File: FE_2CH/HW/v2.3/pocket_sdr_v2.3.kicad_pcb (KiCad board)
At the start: 4 copper layers, 55 x 21.6 mm, 80 parts, among them J1 PINH_2MM_2P, J2 USB_C_Receptacle_USB2.0, J4 SMA-ANG, U1 MAX2771, U2 MAX2771, U3 CY7C68013A-56LTXCT, U4 AT24C128C, U5 LDO 3.3V 500mA SOT23-5

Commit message: Fix USB-C footprint assignment
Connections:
- C10 pad 2: GND -> CPAD_2.2MM
- C11 pad 2: GND -> CPAD_2.2MM
- C13 pad 2: GND -> CPAD_2.2MM
- C14 pad 1: GND -> CPAD_2.2MM
- C16 pad 2: GND -> CPAD_2.2MM
- C17 pad 2: GND -> CPAD_2.2MM
- C18 pad 2: GND -> CPAD_2.2MM
- C19 pad 1: GND -> CPAD_2.2MM
- C2 pad 1: GND -> CPAD_2.2MM
- C20 pad 1: GND -> CPAD_2.2MM
- C21 pad 2: GND -> CPAD_2.2MM
- C22 pad P$2: GND -> CPAD_2.2MM
- C23 pad 2: GND -> CPAD_2.2MM
- C24 pad P$2: GND -> CPAD_2.2MM
- C25 pad 2: GND -> CPAD_2.2MM
- C26 pad 2: GND -> CPAD_2.2MM
- C27 pad 2: GND -> CPAD_2.2MM
- C28 pad 2: GND -> CPAD_2.2MM
- C29 pad 2: GND -> CPAD_2.2MM
- C30 pad 2: GND -> CPAD_2.2MM
- C31 pad 2: GND -> CPAD_2.2MM
- C32 pad 2: GND -> CPAD_2.2MM
- C33 pad 2: GND -> CPAD_2.2MM
- C34 pad 2: GND -> CPAD_2.2MM
- C35 pad 2: GND -> CPAD_2.2MM
- C36 pad 2: GND -> CPAD_2.2MM
- C37 pad 2: GND -> CPAD_2.2MM
- C38 pad 2: GND -> CPAD_2.2MM
- C39 pad 2: GND -> CPAD_2.2MM
- C4 pad 2: GND -> CPAD_2.2MM
- C40 pad 2: GND -> CPAD_2.2MM
- C41 pad 2: GND -> CPAD_2.2MM
- C42 pad 2: GND -> CPAD_2.2MM
- C43 pad 1: GND -> CPAD_2.2MM
- C6 pad 2: GND -> CPAD_2.2MM
- C7 pad 2: GND -> CPAD_2.2MM
- J2 pad A1: GND -> CPAD_2.2MM
- J2 pad A12: GND -> CPAD_2.2MM
- J2 pad B1: GND -> CPAD_2.2MM
- J2 pad B12: GND -> CPAD_2.2MM
- J2 pad S1: GND -> CPAD_2.2MM
- J4 pad P2: GND -> CPAD_2.2MM
- J4 pad P3: GND -> CPAD_2.2MM
- J4 pad P4: GND -> CPAD_2.2MM
- J4 pad P5: GND -> CPAD_2.2MM
- LED1 pad 2: GND -> CPAD_2.2MM
- LED2 pad 2: GND -> CPAD_2.2MM
- LED3 pad 2: GND -> CPAD_2.2MM
- R12 pad 1: GND -> CPAD_2.2MM
- R13 pad 1: GND -> CPAD_2.2MM
- RF-SHEILD-CASE0 pad P1: GND -> CPAD_2.2MM
- RF-SHEILD-CASE0 pad P10: GND -> CPAD_2.2MM
- RF-SHEILD-CASE0 pad P11: GND -> CPAD_2.2MM
- RF-SHEILD-CASE0 pad P12: GND -> CPAD_2.2MM
- RF-SHEILD-CASE0 pad P2: GND -> CPAD_2.2MM
- RF-SHEILD-CASE0 pad P3: GND -> CPAD_2.2MM
- RF-SHEILD-CASE0 pad P4: GND -> CPAD_2.2MM
- RF-SHEILD-CASE0 pad P5: GND -> CPAD_2.2MM
- RF-SHEILD-CASE0 pad P6: GND -> CPAD_2.2MM
- RF-SHEILD-CASE0 pad P7: GND -> CPAD_2.2MM
- RF-SHEILD-CASE0 pad P8: GND -> CPAD_2.2MM
- RF-SHEILD-CASE0 pad P9: GND -> CPAD_2.2MM
- RF_DIVIDER0 pad 1: GND -> CPAD_2.2MM
- RF_DIVIDER0 pad 3: GND -> CPAD_2.2MM
- RF_DIVIDER0 pad 5: GND -> CPAD_2.2MM
- TCXO0 pad 1: GND -> CPAD_2.2MM
- TCXO0 pad 2: GND -> CPAD_2.2MM
- U1 pad 20: GND -> CPAD_2.2MM
- U1 pad 26: GND -> CPAD_2.2MM
- U1 pad 5: GND -> CPAD_2.2MM
- U1 pad C1: GND -> CPAD_2.2MM
- U1 pad C2: GND -> CPAD_2.2MM
- U1 pad C3: GND -> CPAD_2.2MM
- U1 pad C4: GND -> CPAD_2.2MM
- U1 pad EP: GND -> CPAD_2.2MM
- U1 pad V1: GND -> CPAD_2.2MM
- U1 pad V2: GND -> CPAD_2.2MM
- U1 pad V3: GND -> CPAD_2.2MM
- U1 pad V4: GND -> CPAD_2.2MM
- U1 pad V5: GND -> CPAD_2.2MM
- U1 pad V6: GND -> CPAD_2.2MM
- U1 pad V7: GND -> CPAD_2.2MM
- U1 pad V8: GND -> CPAD_2.2MM
- U1 pad V9: GND -> CPAD_2.2MM
- U2 pad 19: GND -> CPAD_2.2MM
- U2 pad 25: GND -> CPAD_2.2MM
- U2 pad C1: GND -> CPAD_2.2MM
- U2 pad C2: GND -> CPAD_2.2MM
- U2 pad C3: GND -> CPAD_2.2MM
- U2 pad C4: GND -> CPAD_2.2MM
- U2 pad EP: GND -> CPAD_2.2MM
- U2 pad V1: GND -> CPAD_2.2MM
- U2 pad V2: GND -> CPAD_2.2MM
- U2 pad V3: GND -> CPAD_2.2MM
- U2 pad V4: GND -> CPAD_2.2MM
- U2 pad V5: GND -> CPAD_2.2MM
- U2 pad V6: GND -> CPAD_2.2MM
- U2 pad V7: GND -> CPAD_2.2MM
- U2 pad V8: GND -> CPAD_2.2MM
- U2 pad V9: GND -> CPAD_2.2MM
- U3 pad EP1: GND -> CPAD_2.2MM
- U3 pad EP2: GND -> CPAD_2.2MM
- U3 pad EP3: GND -> CPAD_2.2MM
- U3 pad EP4: GND -> CPAD_2.2MM
- U3 pad EP5: GND -> CPAD_2.2MM
- U3 pad P$1: GND -> CPAD_2.2MM
- U3 pad P$10: GND -> CPAD_2.2MM
- U3 pad P$11: GND -> CPAD_2.2MM
- U3 pad P$12: GND -> CPAD_2.2MM
- U3 pad P$13: GND -> CPAD_2.2MM
- U3 pad P$14: GND -> CPAD_2.2MM
- U3 pad P$15: GND -> CPAD_2.2MM
- U3 pad P$16: GND -> CPAD_2.2MM
- U3 pad P$17: GND -> CPAD_2.2MM
- U3 pad P$18: GND -> CPAD_2.2MM
- U3 pad P$19: GND -> CPAD_2.2MM
- U3 pad P$2: GND -> CPAD_2.2MM
- U3 pad P$20: GND -> CPAD_2.2MM
- U3 pad P$3: GND -> CPAD_2.2MM
- U3 pad P$4: GND -> CPAD_2.2MM
- U3 pad P$5: GND -> CPAD_2.2MM
- U3 pad P$6: GND -> CPAD_2.2MM
- U3 pad P$7: GND -> CPAD_2.2MM
- U3 pad P$8: GND -> CPAD_2.2MM
- U3 pad P$9: GND -> CPAD_2.2MM
- U3 pad P10: GND -> CPAD_2.2MM
- U3 pad P12: GND -> CPAD_2.2MM
- U3 pad P14: GND -> CPAD_2.2MM
- U3 pad P2: GND -> CPAD_2.2MM
- U3 pad P26: GND -> CPAD_2.2MM
- U3 pad P28: GND -> CPAD_2.2MM
- U3 pad P37: GND -> CPAD_2.2MM
- U3 pad P41: GND -> CPAD_2.2MM
- U3 pad P53: GND -> CPAD_2.2MM
- U3 pad P56: GND -> CPAD_2.2MM
- U3 pad P6: GND -> CPAD_2.2MM
- U4 pad 2: GND -> CPAD_2.2MM
- U4 pad 3: GND -> CPAD_2.2MM
- U4 pad 4: GND -> CPAD_2.2MM
- U4 pad 7: GND -> CPAD_2.2MM
- U5 pad 2: GND -> CPAD_2.2MM
- XTAL0 pad P2: GND -> CPAD_2.2MM
- XTAL0 pad P4: GND -> CPAD_2.2MM
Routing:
- net GND: track 1.18 -> 0.00 mm, vias 155 -> 0
- net CPAD_2.2MM: track 0.00 -> 1.18 mm, vias 0 -> 155
- added copper zone on B.Cu, net CPAD_2.2MM
- added copper zone on F.Cu, net CPAD_2.2MM
- added copper zone on In1.Cu, net CPAD_2.2MM
- added copper zone on In2.Cu, net CPAD_2.2MM
- removed copper zone on B.Cu, net GND
- removed copper zone on F.Cu, net GND
- removed copper zone on In1.Cu, net GND
- removed copper zone on In2.Cu, net GND

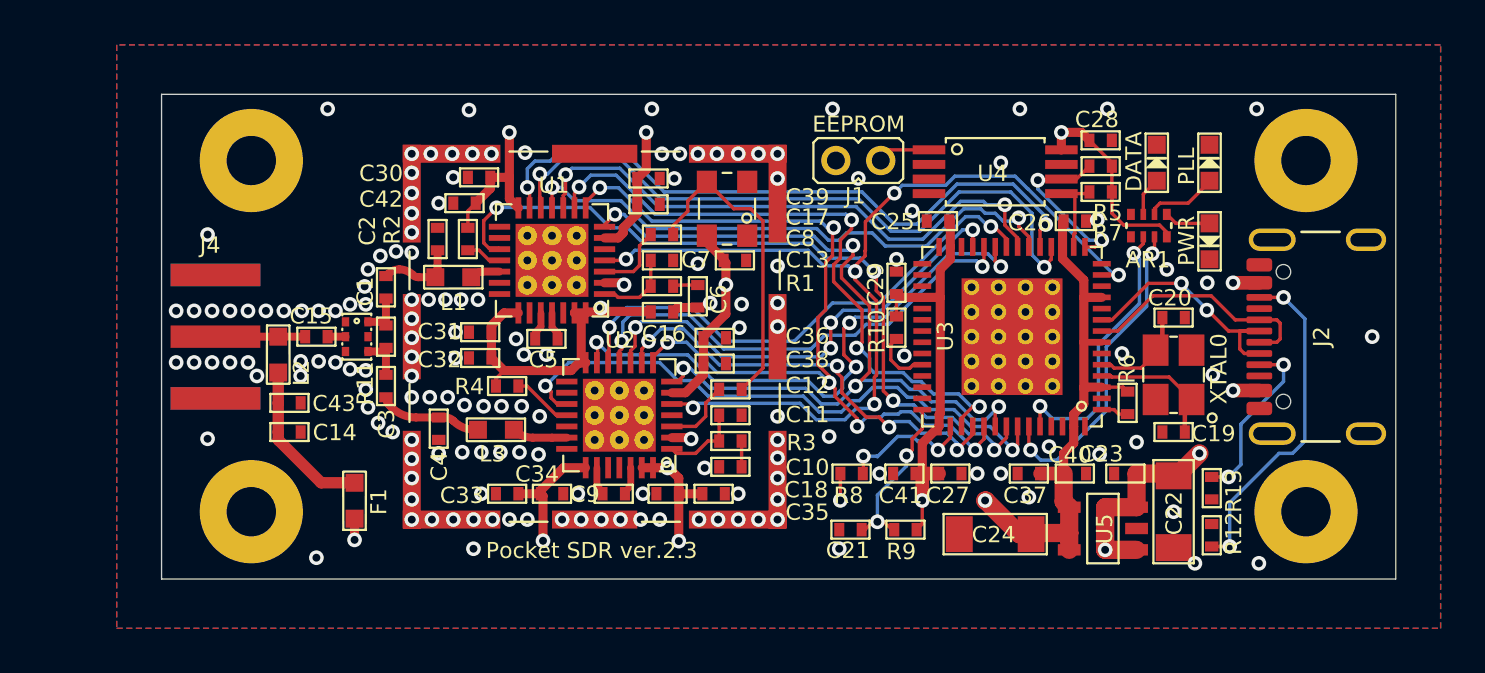
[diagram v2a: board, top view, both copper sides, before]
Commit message: Put back bias tee and U.FL connector
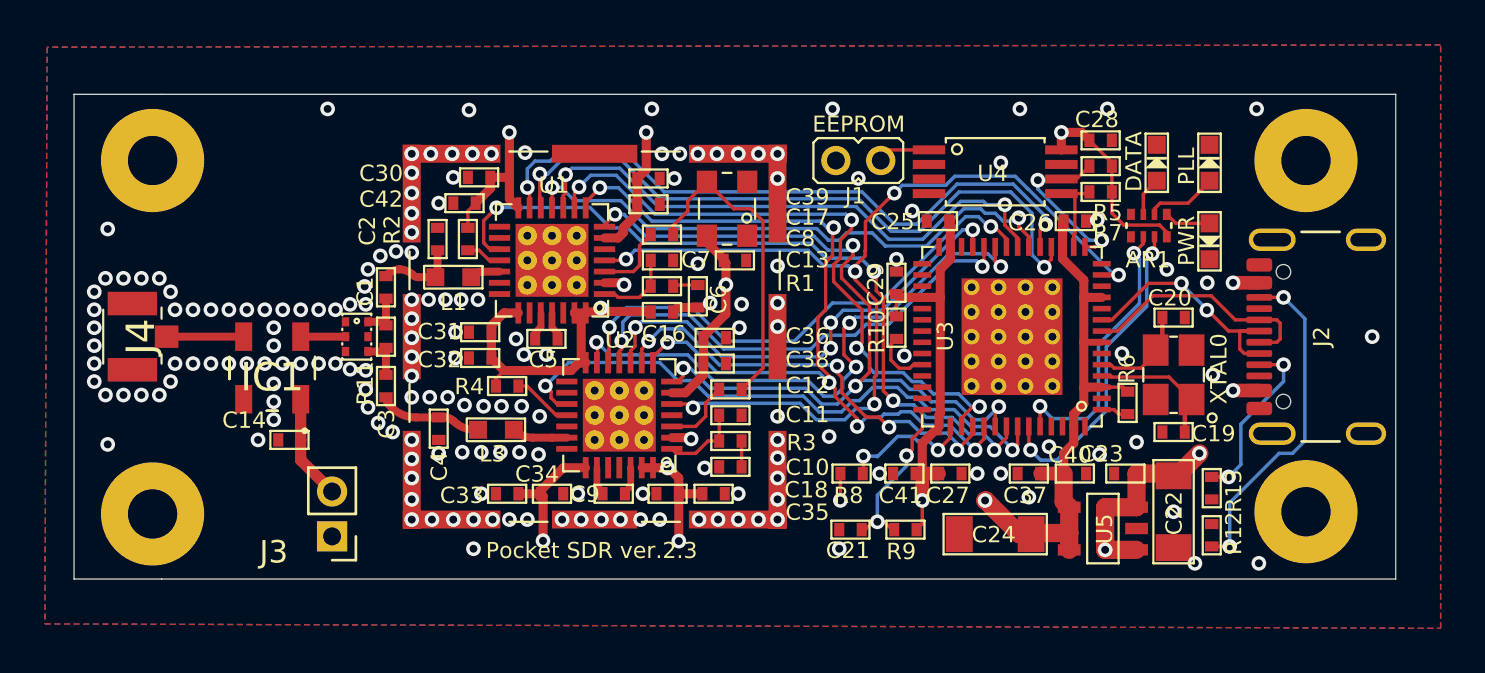
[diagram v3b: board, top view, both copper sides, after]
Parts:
- removed C15: 470pF, pocket_sdr_v2.3:C1005
- removed C43: 0.1uF, pocket_sdr_v2.3:C1005
- removed F1: 12V 8 Ohm, Trip 250mA, pocket_sdr_v2.3:C1608
- removed L2: 68nH, pocket_sdr_v2.3:C1608
- added IC1: TCBT-2R5G+, LIB_TCBT-2R5G+:TCBT2R5G, F.Cu at (125.9, 107.3)
- added J3: ANT POWER, Connector_PinHeader_2.00mm:PinHeader_1x02_P2.00mm_Vertical, F.Cu at (128.6, 114.8)
- C14: value 100pF -> 0.01uF
- J4: value SMA-ANG -> U.FL-R-SMT-1_80_; footprint pocket_sdr_v2.3:SMA-ANG -> LIB_U.FL-R-SMT-1_80_:UFLRSMT180
- moved #PAD02 4.40 mm to (120.6, 113.8)
- moved #PAD01 4.40 mm to (120.6, 98.1)
- moved J4 0.41 mm to (119.8, 106.0)
- moved C14 0.35 mm to (126.7, 110.5), turned to 0 degrees
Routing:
- net Net-(J4-RF): track 4.00 -> 0.00 mm
- net Net-(IC1-RF&DC): track 0.00 -> 3.24 mm
- net Net-(IC1-DC): track 7.19 -> 4.69 mm
- net Net-(IC1-RF): track 0.80 -> 2.00 mm
- net /5V: track 55.0 -> 55.1 mm, vias 5 -> 4
- net CPAD_2.2MM: vias 155 -> 176
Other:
- board size 55 x 21.6 mm -> 58.9 x 21.6 mm
